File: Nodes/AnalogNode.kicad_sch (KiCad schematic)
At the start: 19 parts, among them T2 Conn_01x01, U2 STM32H7B0RBT6, Y2 ASE-25.000MHZ-LC-T

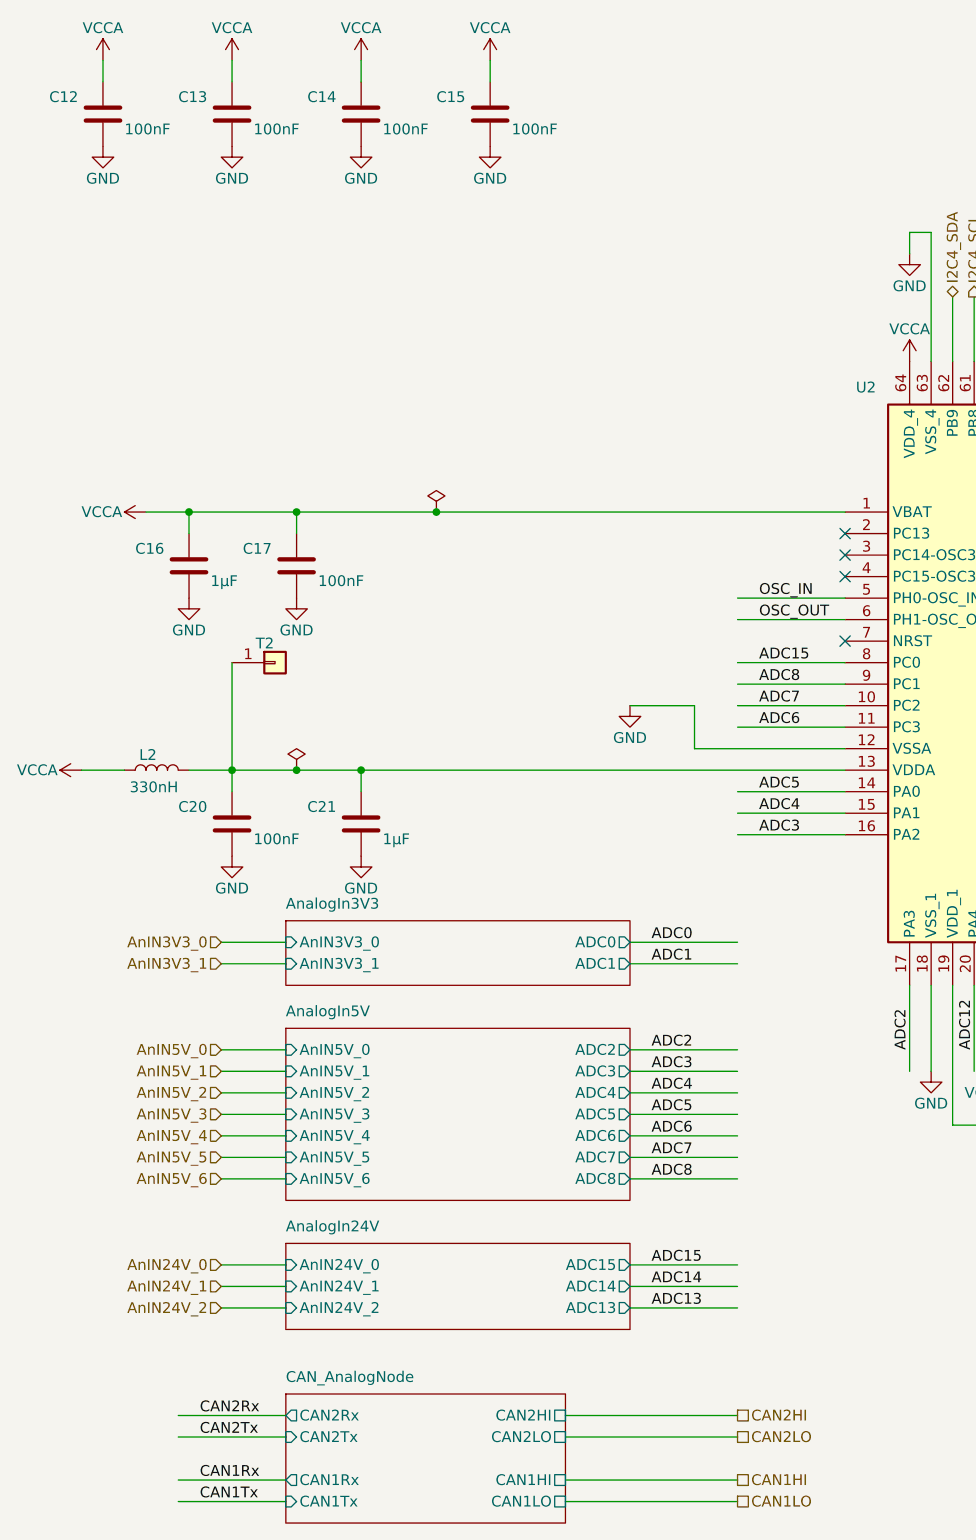
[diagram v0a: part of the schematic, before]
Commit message: Nodes v2.1.2 Improved
- Improved schematic design
- Added two 4.7 uF caps according to the datasheets of the microchips
- Other small changes
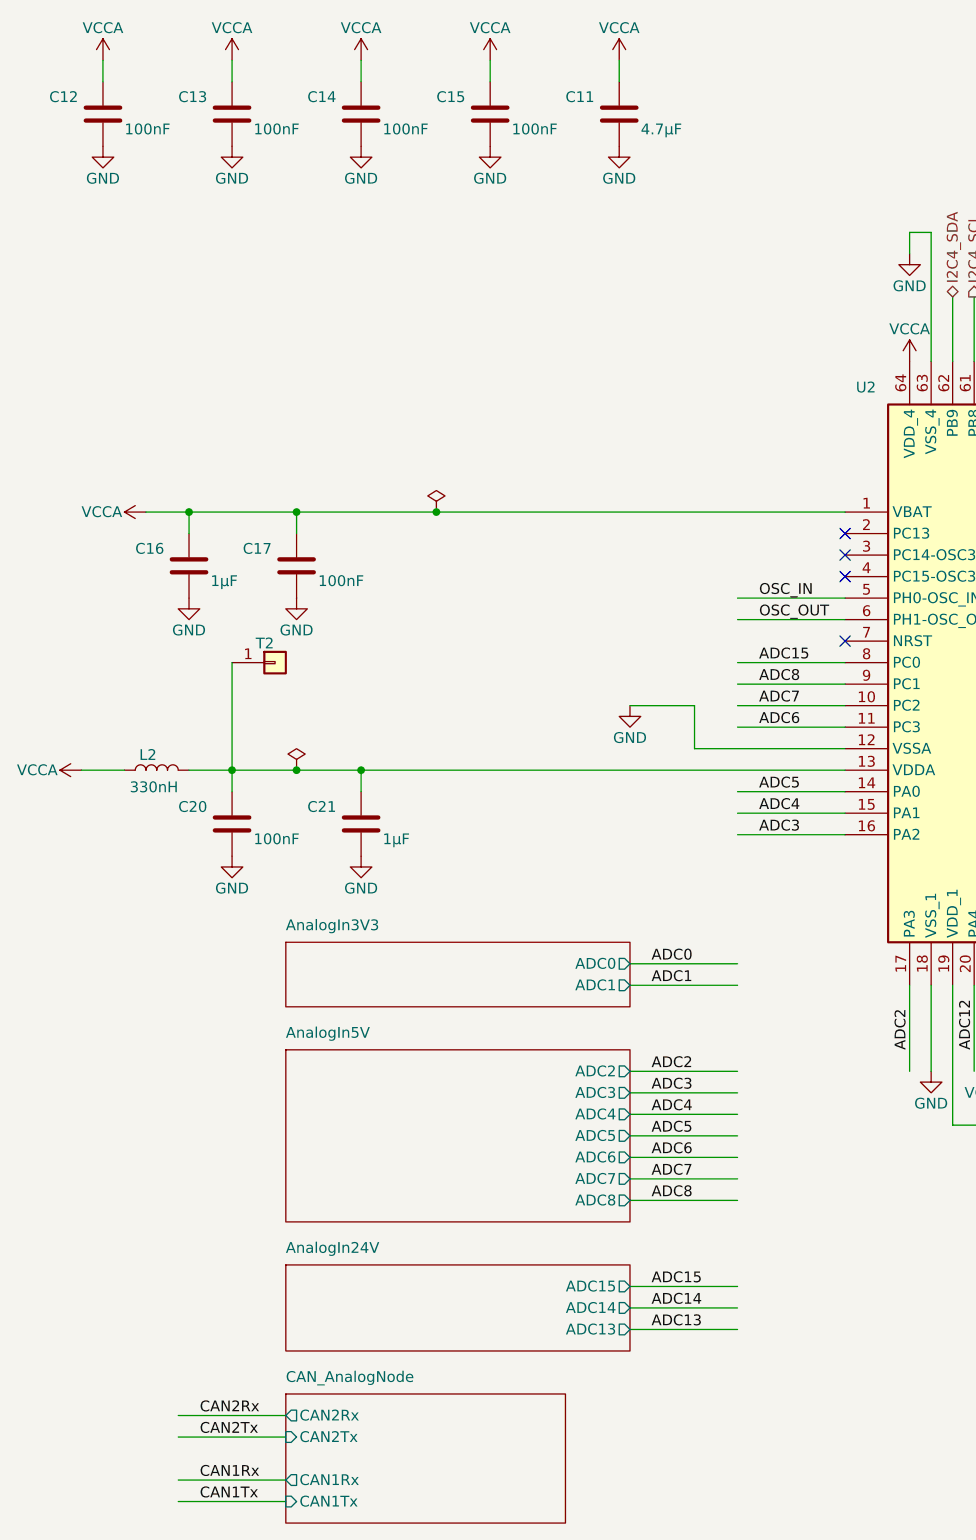
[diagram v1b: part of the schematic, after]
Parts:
- added C11: 4.7µF, Capacitor_SMD:C_0805_2012Metric_Pad1.18x1.45mm_HandSolder, symbol Device:C
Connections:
- net GND: now also C11.2
- net VCCA: now also C11.1
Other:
- sheet AnalogIn24V ports: added none; removed AnIN24V_0, AnIN24V_1, AnIN24V_2
- sheet AnalogIn3V3 ports: added none; removed AnIN3V3_0, AnIN3V3_1
- sheet AnalogIn5V ports: added none; removed AnIN5V_0, AnIN5V_1, AnIN5V_2, AnIN5V_3, AnIN5V_4, AnIN5V_5, AnIN5V_6
- sheet CAN_AnalogNode ports: added none; removed CAN1HI, CAN1LO, CAN2HI, CAN2LO

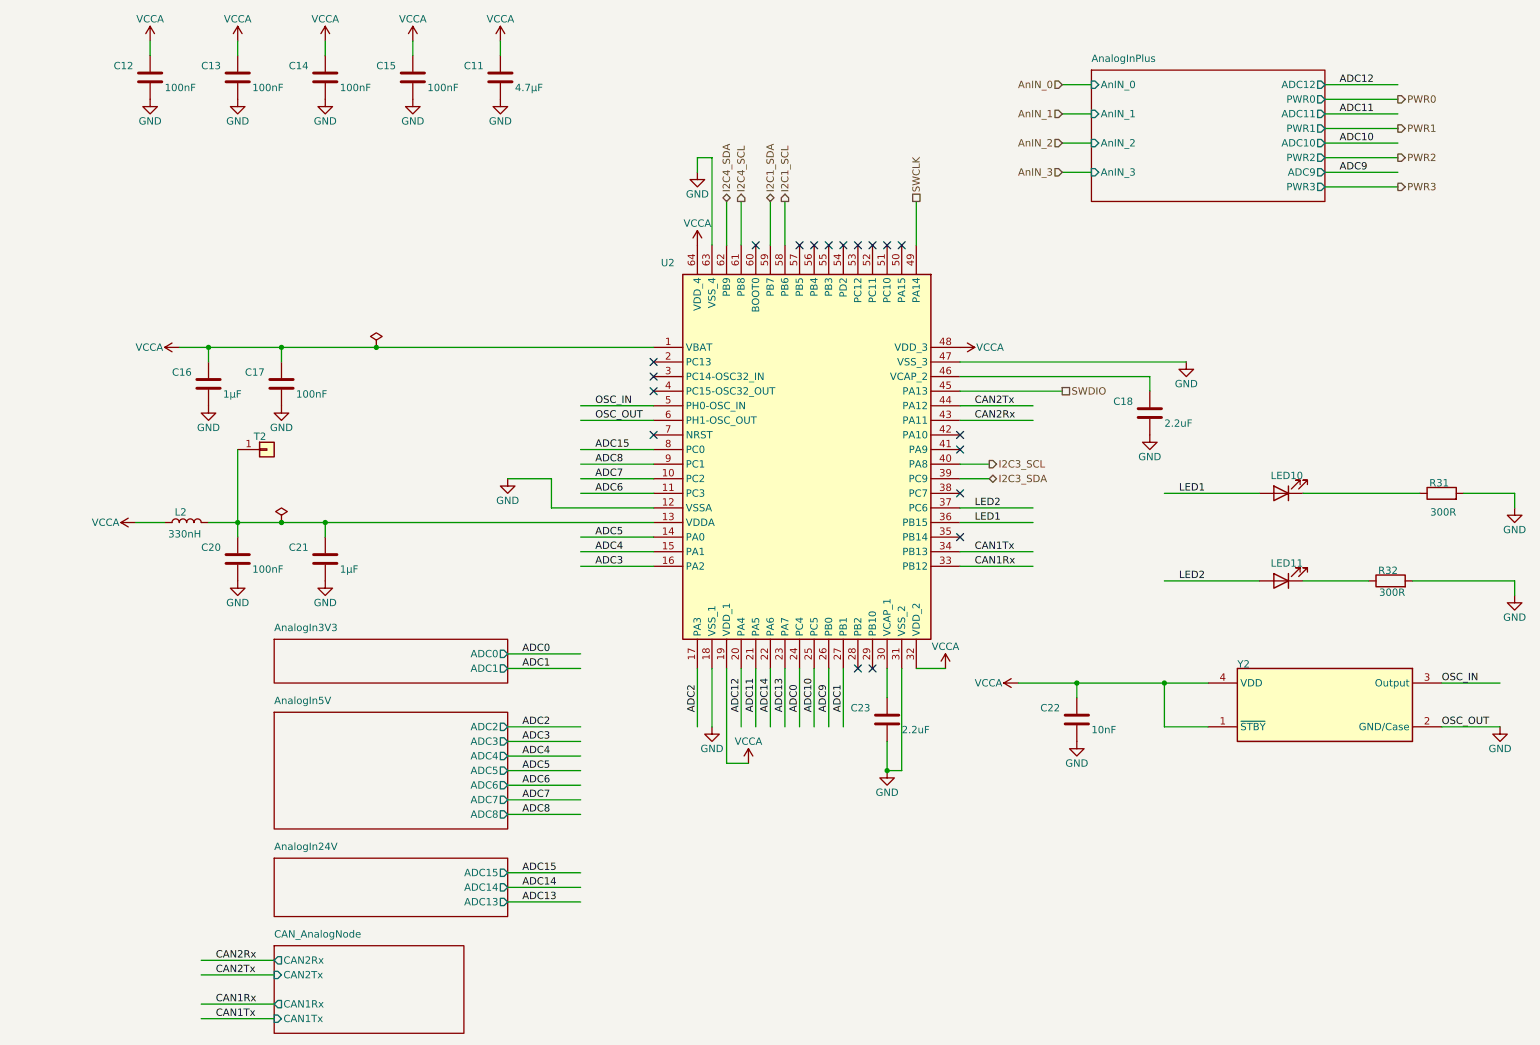
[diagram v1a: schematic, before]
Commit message: Nodes v2.2
- This version not compatible with BOB v.2.1.2 and older!
- Completely new layout design
- New power supply system with new voltage regulators
- New microchip STM32G431RBTx for the Analog Node
- New connection system (instead of 18 pin headers now 8 pin and pins were grouped by functions)
- Reduced size of the board by 5%
- Removed power switch for the Analog Node (because this functionality is now provided by a separate voltage regulator. for a more stable voltage)
- Removable ground from the holes added
- Layer numbers added
- Small improvements of the components information were made
- New oscillator for the Nodes
- Removed CAN1, so now only one CAN connection due to the capabilities of the new microchip
- Other small changes and fixes on the schematic and design
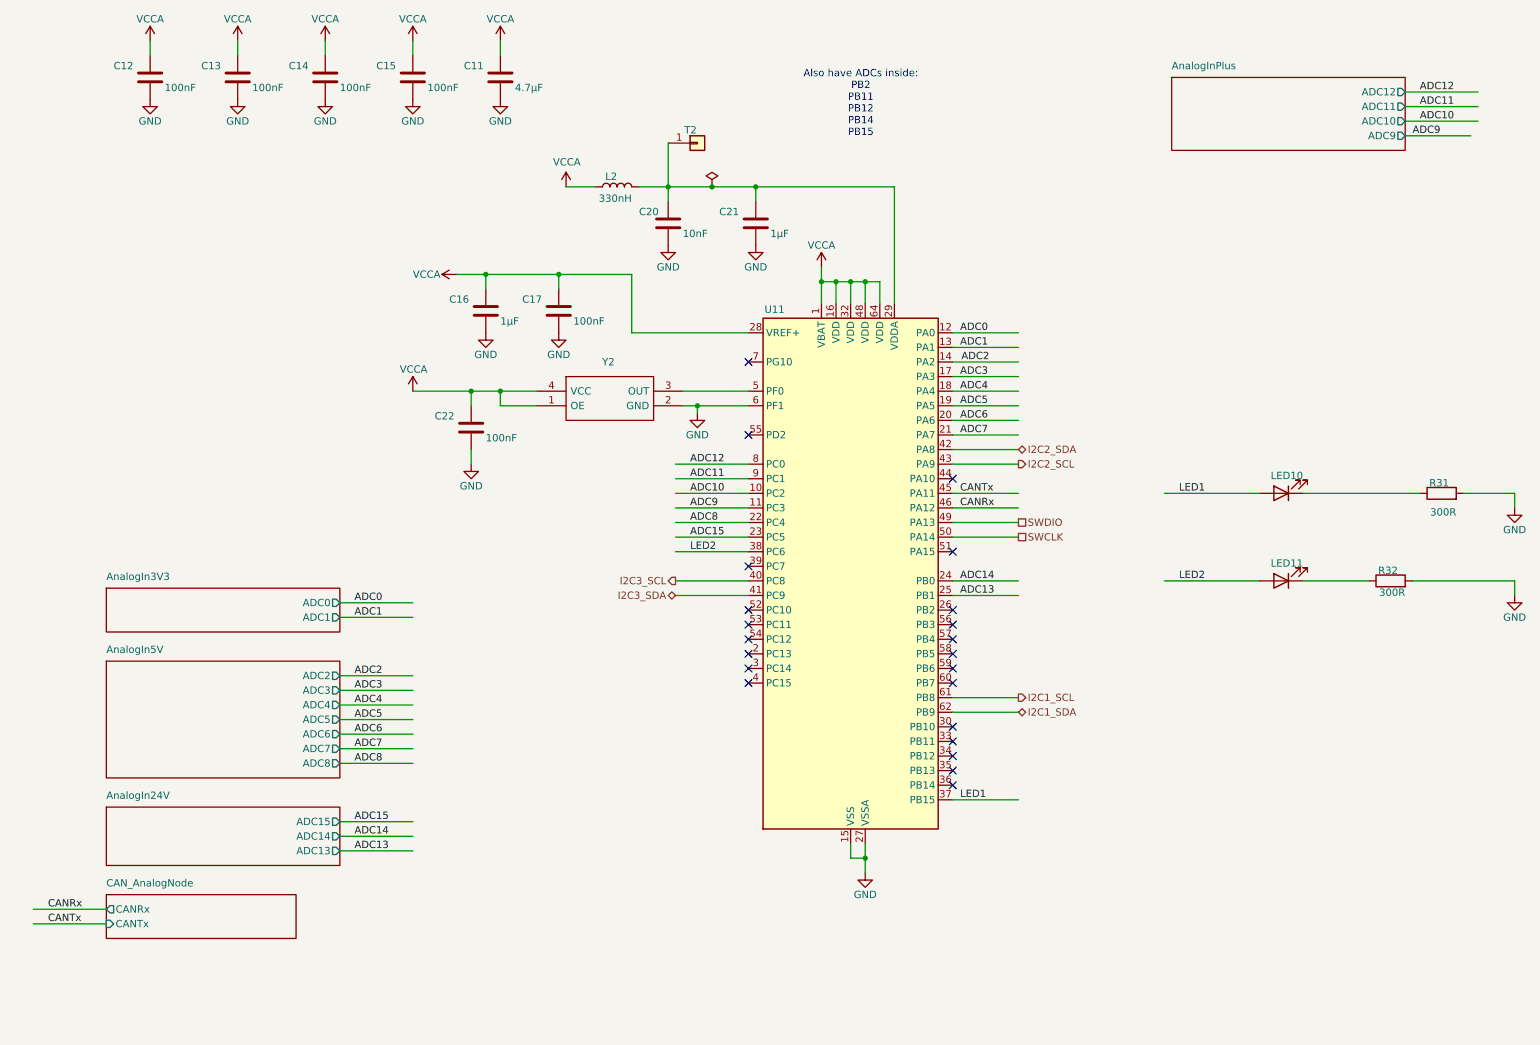
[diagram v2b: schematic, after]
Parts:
- removed C18, C23: 2.2uF, Capacitor_SMD:C_0805_2012Metric_Pad1.18x1.45mm_HandSolder, symbol Device:C
- removed U2: STM32H7B0RBT6, SamacSys.PcbLib:QFP50P1200X1200X160-64N, symbol Untitled-altium-import:root_0_STM32H7B0RBT6
- removed Y2: ASE-25.000MHZ-LC-T, Vault:FP-ASE-MFG, symbol Untitled-altium-import:root_0_61a724e6190563596ac712fef61ad37
- added U11: STM32G431RBTx, Package_QFP:LQFP-64_10x10mm_P0.5mm, symbol MCU_ST_STM32G4:STM32G431RBTx
- added Y2: SG-8018CE_8.0000M-TJHPA3, Oscillator:SG8018CE80000MTJHPA3, symbol Oscillator:SG-8018CE_8.0000M-TJHPA3
- C20: value 100nF -> 10nF; ALTIUM_VALUE 100nF -> 10nF; HEIGHT 0.94mm -> 0.78mm; LENGTH 2.01mm -> 2mm; RATED DC VOLTAGE (URDC) 50V -> 250V; REFERENCE STANDARD (none) -> AEC-Q200
- C22: value 10nF -> 100nF; ALTIUM_VALUE 10nF -> 100nF; HEIGHT 0.78mm -> 0.94mm; LENGTH 2mm -> 2.01mm; RATED DC VOLTAGE (URDC) 250V -> 50V; REFERENCE STANDARD AEC-Q200 -> (none)
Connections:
- net ADC0: now also U11.12 (PA0)
- net ADC1: now also U11.13 (PA1)
- net ADC10: now also U11.10 (PC2)
- net ADC11: now also U11.9 (PC1)
- net ADC12: now also U11.8 (PC0)
- net ADC13: now also U11.25 (PB1)
- net ADC14: now also U11.24 (PB0)
- net ADC15: now also U11.23 (PC5)
- net ADC2: now also U11.14 (PA2)
- net ADC3: now also U11.17 (PA3)
- net ADC4: now also U11.18 (PA4)
- net ADC5: now also U11.19 (PA5)
- net ADC6: now also U11.20 (PA6)
- net ADC7: now also U11.21 (PA7)
- net ADC8: now also U11.22 (PC4)
- net ADC9: now also U11.11 (PC3)
- net GND: now also U11.15 (VSS), U11.27 (VSSA), U11.31 (VSS), U11.47 (VSS), U11.6 (PF1), U11.63 (VSS), Y2.2 (GND)
- net I2C1_SCL: now also U11.61 (PB8)
- net I2C1_SDA: now also U11.62 (PB9)
- net I2C3_SCL: now also U11.40 (PC8)
- net I2C3_SDA: now also U11.41 (PC9)
- net LED1: now also U11.37 (PB15)
- net LED2: now also U11.38 (PC6)
- net SWCLK: now also U11.50 (PA14)
- net SWDIO: now also U11.49 (PA13)
- net VCCA: now also U11.1 (VBAT), U11.16 (VDD), U11.28 (VREF+), U11.32 (VDD), U11.48 (VDD), U11.64 (VDD), Y2.1 (OE), Y2.4 (VCC)
- net at C20.1, C21.1, L2.2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: now also U11.29 (VDDA)
- new net: U11.5 (PF0), Y2.3 (OUT)
- new net CANRx: U11.46 (PA12)
- new net CANTx: U11.45 (PA11)
- new net I2C2_SCL: U11.43 (PA9)
- new net I2C2_SDA: U11.42 (PA8)
- no-connect marks 19 -> 22
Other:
- sheet AnalogInPlus ports: added none; removed AnIN_0, AnIN_1, AnIN_2, AnIN_3, PWR0, PWR1, PWR2, PWR3
- sheet CAN_AnalogNode ports: added CANRx, CANTx; removed CAN1Rx, CAN1Tx, CAN2Rx, CAN2Tx
- note added: "Also have ADCs inside: PB2 PB11 PB12 PB14 PB15"

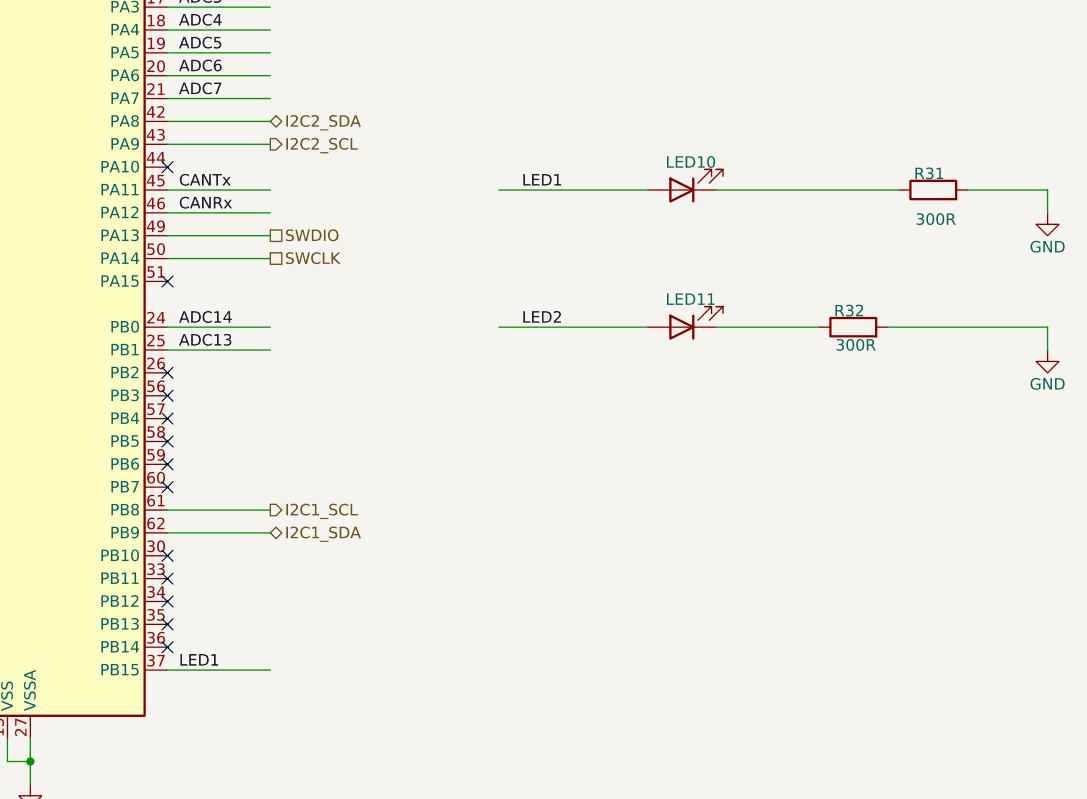
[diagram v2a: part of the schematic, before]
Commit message: Nodes v2.2.3
- Added one more PWM Level shifter
- Controllable amplitude of PWM by switches
- Added labels
- Added resistors to solve BOOT issue
- I2C1 pins changed
- More GND vias
- Higher resistance for adjustable voltage regulators
- Other small changes
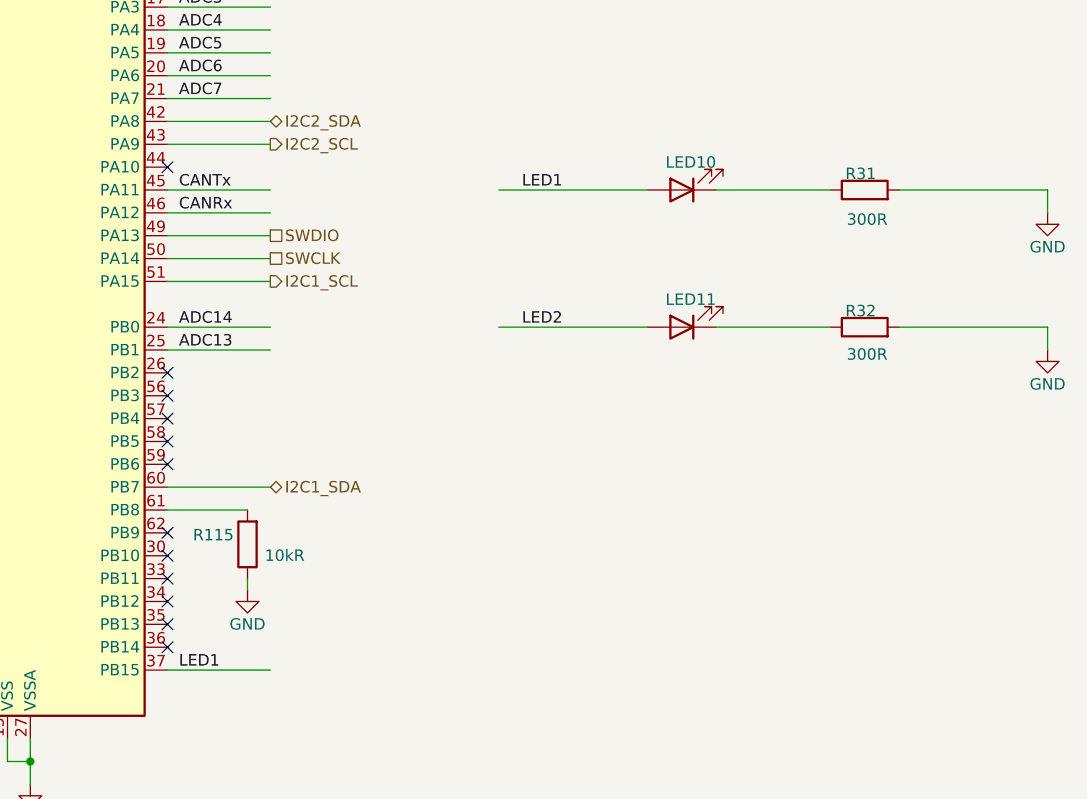
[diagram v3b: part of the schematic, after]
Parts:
- added R115: 10kR, Resistor_SMD:R_0805_2012Metric_Pad1.20x1.40mm_HandSolder, symbol Device:R
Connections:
- net GND: now also R115.1
- net I2C1_SCL: now also U11.51 (PA15); no longer U11.61 (PB8)
- net I2C1_SDA: now also U11.60 (PB7); no longer U11.62 (PB9)
- new net: R115.2, U11.61 (PB8)
- no-connect marks 22 -> 21
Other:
- moved on the sheet: R31, R32
